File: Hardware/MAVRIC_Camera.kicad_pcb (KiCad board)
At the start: 2 copper layers, 65 x 50 mm, 13 parts, among them J1 MASTER, J2 CAMERA, J3 SERVO, J4 ICSP-PIC, J5 USB, U1 AOZ1031

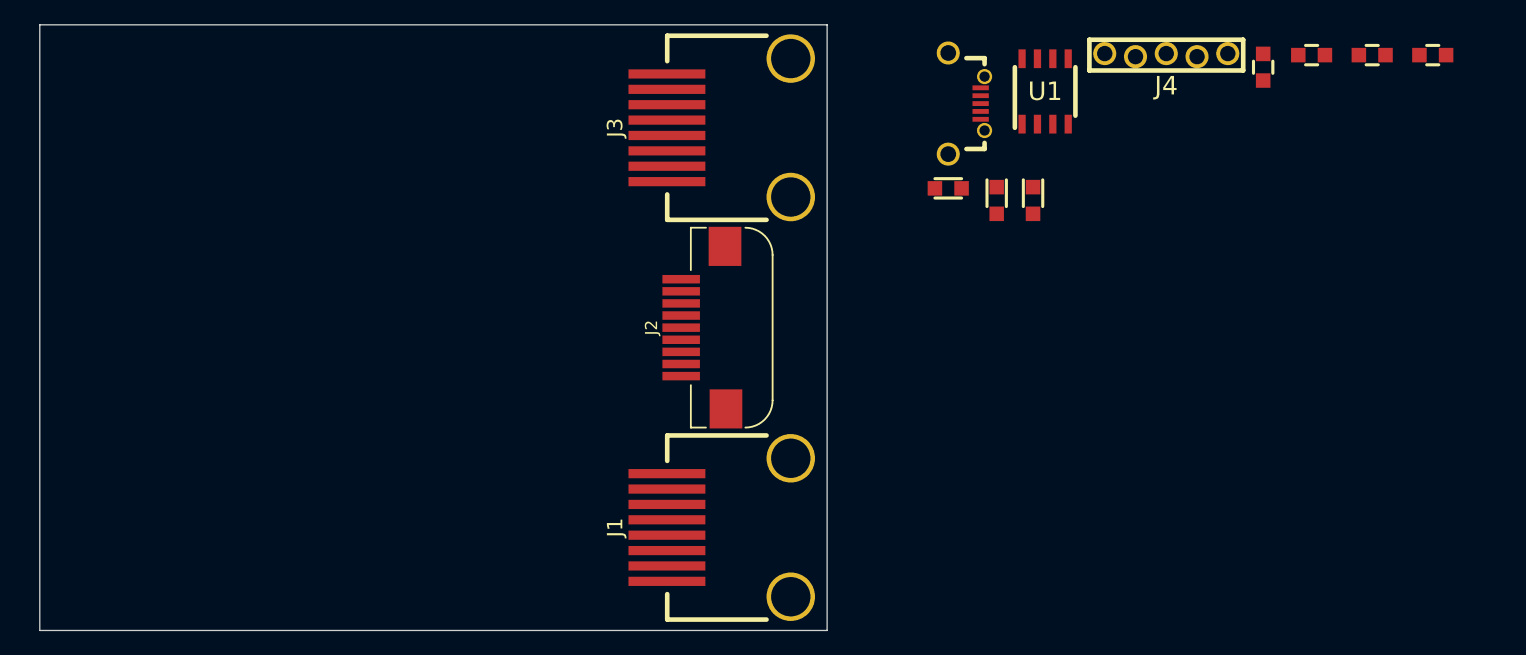
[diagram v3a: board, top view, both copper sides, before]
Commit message: Finish schematic
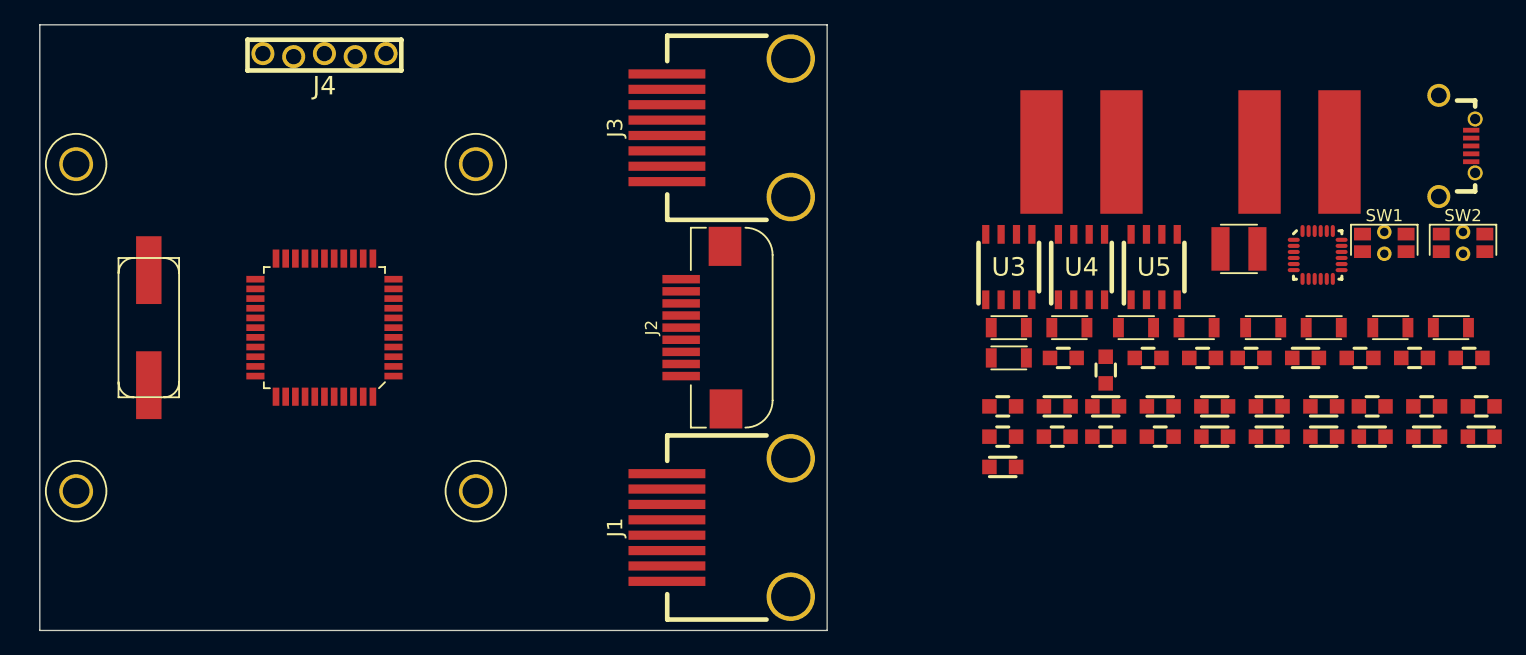
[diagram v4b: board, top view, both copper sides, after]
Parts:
- added C10: 0.1uF, CAPC2012, F.Cu at (239.5, 120.0)
- added C11: 10uF, CAPC2012, F.Cu at (244.0, 122.5)
- added C12: 0.1uF, CAPC2012, F.Cu at (248.5, 122.5)
- added C13: 0.1uF, CAPC2012, F.Cu at (253.0, 122.5)
- added C14: 0.1uF, CAPC2012, F.Cu at (253.0, 120.0)
- added C15: 22uF, CAPC3216, F.Cu at (248.0, 113.5)
- added C16: 22uF, CAPC3216, F.Cu at (253.0, 113.5)
- added C17: C, CAPC2012, F.Cu at (248.5, 120.0)
- added C18: 22uF, CAPC3216, F.Cu at (227.0, 116.0)
- added C19: 22uF, CAPC3216, F.Cu at (242.5, 113.5)
- added C20: C, CAPC2012, F.Cu at (244.0, 120.0)
- added C21: 22uF, CAPC3216, F.Cu at (258.5, 113.5)
- added C22: 22uF, CAPC3216, F.Cu at (227.0, 113.5)
- added C23: 22uF, CAPC3216, F.Cu at (237.5, 113.5)
- added C4: 10nF, CAPC2012, F.Cu at (257.0, 122.5)
- added C5: 0.1uF, CAPC2012, F.Cu at (261.5, 122.5)
- added C6: 0.1uF, CAPC2012, F.Cu at (266.0, 122.5)
- added C7: 2.2nF, CAPC2012, F.Cu at (226.5, 125.0)
- added C8: 18pF, CAPC2012, F.Cu at (235.0, 120.0)
- added C9: 18pF, CAPC2012, F.Cu at (231.0, 120.0)
- added L1: 33uH, INDC-SRN4018, F.Cu at (246.0, 107.0)
- added L2: 22uH, INDC-SRN1060, F.Cu at (251.0, 99.0)
- added L3: 22uH, INDC-SRN1060, F.Cu at (233.0, 99.0)
- added MECH-HOLE220: VAL**, MECH-HOLE220, F.Cu at (150.0, 100.0)
- added MECH-HOLE220: VAL**, MECH-HOLE220, F.Cu at (150.0, 127.0)
- added MECH-HOLE220: VAL**, MECH-HOLE220, F.Cu at (183.0, 127.0)
- added MECH-HOLE220: VAL**, MECH-HOLE220, F.Cu at (183.0, 100.0)
- added R10: 10k, RESC2012, F.Cu at (226.5, 122.5)
- added R11: R, RESC2012, F.Cu at (231.0, 122.5)
- added R12: R, RESC2012, F.Cu at (235.0, 122.5)
- added R13: 10k, RESC2012, F.Cu at (231.5, 116.0)
- added R14: R, RESC2012, F.Cu at (266.0, 120.0)
- added R15: R, RESC2012, F.Cu at (257.0, 120.0)
- added R16: R, RESC2012, F.Cu at (261.5, 120.0)
- added R5: 10k, RESC2012, F.Cu at (260.5, 116.0)
- added R6: 10k, RESC2012, F.Cu at (256.0, 116.0)
- added R7: 10k, RESC2012, F.Cu at (226.5, 120.0)
- added R8: 10k, RESC2012, F.Cu at (265.0, 116.0)
- added R9: R, RESC2012, F.Cu at (239.5, 122.5)
- added SW1: PRGM, SW-EVQP7, F.Cu at (258.0, 106.5)
- added SW2: RESET, SW-EVQP7, F.Cu at (264.5, 106.5)
- added U2: MPU9150, PQFN50P400X400X110-24N, F.Cu at (252.5, 107.5)
- added U3: AOZ1031, SOIC127P600X175-8N, F.Cu at (227.0, 108.5)
- added U4: AOZ1031, SOIC127P600X175-8N, F.Cu at (233.0, 108.5)
- added U5: AOZ1031, SOIC127P600X175-8N, F.Cu at (239.0, 108.5)
- added X1: 8MHz, HC49-US, F.Cu at (156.0, 113.5)
- C1, C2: value CP -> 22uF; footprint CAPCP2012 -> CAPC3216
- J5: value USB -> USB_MINI
- R2: value R -> 10k
- U1: value AOZ1031 -> PIC32MX250F128D; footprint SOIC127P600X175-8N -> QFP80P1200x1200-44N
- moved J4 69.5 mm to (170.5, 91.0)
- moved U1 62.6 mm to (170.5, 113.5), turned to 180 degrees
- moved J5 40.7 mm to (262.5, 98.5)
- moved C2 36.1 mm to (263.5, 113.5), turned to 0 degrees
- moved C3 32.7 mm to (251.5, 116.0)
- moved R4 29.2 mm to (247.0, 116.0)
- moved R3 28.7 mm to (243.0, 116.0)
- moved R2 28.4 mm to (238.5, 116.0)
- moved R1 28.2 mm to (235.0, 117.0)
- moved C1 12.1 mm to (232.0, 113.5), turned to 0 degrees
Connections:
- C1 pad 1: N-000004 -> +3.3V
- C2 pad 1: +BATT -> +3.3V
- J1 pad 2: GND -> AGND
- J1 pad 3: (no net) -> /U1Rx
- J1 pad 6: (no net) -> /U1Tx
- J2 pad 1: (no net) -> /U2Tx
- J2 pad 2: (no net) -> /U2Rx
- J2 pad 4: (no net) -> N-0000028
- J2 pad 7: GND -> AGND
- J3 pad 1: (no net) -> /Pan
- J3 pad 3: (no net) -> /Tilt
- J3 pad 4: N-000004 -> N-0000061
- J3 pad 5: N-000004 -> N-0000061
- J4 pad 1: (no net) -> /~MCLR
- J4 pad 2: (no net) -> +3.3V
- J4 pad 3: (no net) -> GND
- J4 pad 4: (no net) -> /PGD
- J4 pad 5: (no net) -> /PGC
- J5 pad 1: (no net) -> /VBus
- J5 pad 2: (no net) -> /D-
- J5 pad 3: (no net) -> /D+
- J5 pad 5: (no net) -> GND
- R1 pad 1: N-000003 -> N-0000065
- R1 pad 2: N-000004 -> N-0000061
- R3 pad 2: N-000001 -> N-0000063
- R4 pad 2: N-000003 -> N-0000065
- U1 pad 1: GND -> /CamEn
- U1 pad 2: +BATT -> /ServoEn
- U1 pad 3: GND -> /Tilt
- U1 pad 4: N-000003 -> /Pan
- U1 pad 5: N-000001 -> (no net)
- U1 pad 6: /ServoEn -> GND
- U1 pad 7: N-000004 -> /VCap
- U1 pad 8: N-000004 -> /D+

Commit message: Power systems layout
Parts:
- added C24: 22uF, CAPC3216, F.Cu at (191.0, 128.0)
- added C25: 22uF, CAPC3216, F.Cu at (193.5, 128.0)
- L2, L3: footprint INDC-SRN1060 -> INDC-NR8040
- moved SW2 115.5 mm to (149.0, 105.5), turned to 90 degrees
- moved J5 114.5 mm to (149.0, 113.5)
- moved SW1 110.0 mm to (149.0, 92.0), turned to 90 degrees
- moved C2 93.8 mm to (172.0, 134.0), turned to 270 degrees
- moved R14 81.7 mm to (185.5, 134.0)
- moved C3 77.5 mm to (176.5, 96.5), turned to 0 degrees
- moved R16 76.9 mm to (185.5, 132.0), turned to 180 degrees
- moved L1 75.8 mm to (173.5, 129.0), turned to 270 degrees
- moved R4 73.7 mm to (176.5, 94.5)
- moved C17 72.3 mm to (176.5, 113.5)
- moved R15 71.9 mm to (185.5, 128.0), turned to 180 degrees
- moved C15 71.0 mm to (180.5, 135.5)
- moved R3 68.8 mm to (176.5, 98.5)
- moved C21 68.6 mm to (191.0, 101.0), turned to 270 degrees
- moved R9 64.3 mm to (176.5, 109.5), turned to 180 degrees
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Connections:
- net N-0000027 renamed /Lx
- net N-0000030 renamed /CamLx
- net N-0000061 renamed /SevPwr
- net N-0000066 renamed /SevLx
- C16 pad 1: N-0000028 (its old number) -> /CamPwr
- C18 pad 1: N-0000028 (its old number) -> /CamPwr
- J1 pad 1: /Video -> AGND
- J1 pad 2: AGND -> /Video
- J2 pad 4: N-0000028 (its old number) -> /CamPwr
- L2 pad 2: N-0000028 (its old number) -> /CamPwr
- R9 pad 2: N-0000028 (its old number) -> /CamPwr
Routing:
- net AGND: track 0.00 -> 32.3 mm
- net /Video: track 0.00 -> 29.7 mm
- net +BATT: track 0.00 -> 10.9 mm, vias 0 -> 1
- net /SevPwr: track 0.00 -> 9.85 mm
- net N-0000014: track 0.00 -> 4.35 mm
- net /ServoEn: track 0.00 -> 4.35 mm
- net /CamEn: track 0.00 -> 4.35 mm
- net N-0000013: track 0.00 -> 4.12 mm
- net N-0000039: track 0.00 -> 4.12 mm
- net N-0000019: track 0.00 -> 4.12 mm
- net N-0000037: track 0.00 -> 2.28 mm
- net N-0000028: track 0.00 -> 2.28 mm
- net N-0000017: track 0.00 -> 2.28 mm
- net N-0000038: track 0.00 -> 2.00 mm
- net N-0000029: track 0.00 -> 2.00 mm
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- added copper zone on F.Cu, net +3.3V
- added copper zone on F.Cu, net /CamLx
- added copper zone on F.Cu, net /CamPwr
- added copper zone on F.Cu, net /Lx
- added copper zone on F.Cu, net /SevLx
- added copper zone on F.Cu, net /SevPwr
- added copper zone on F.Cu, net GND

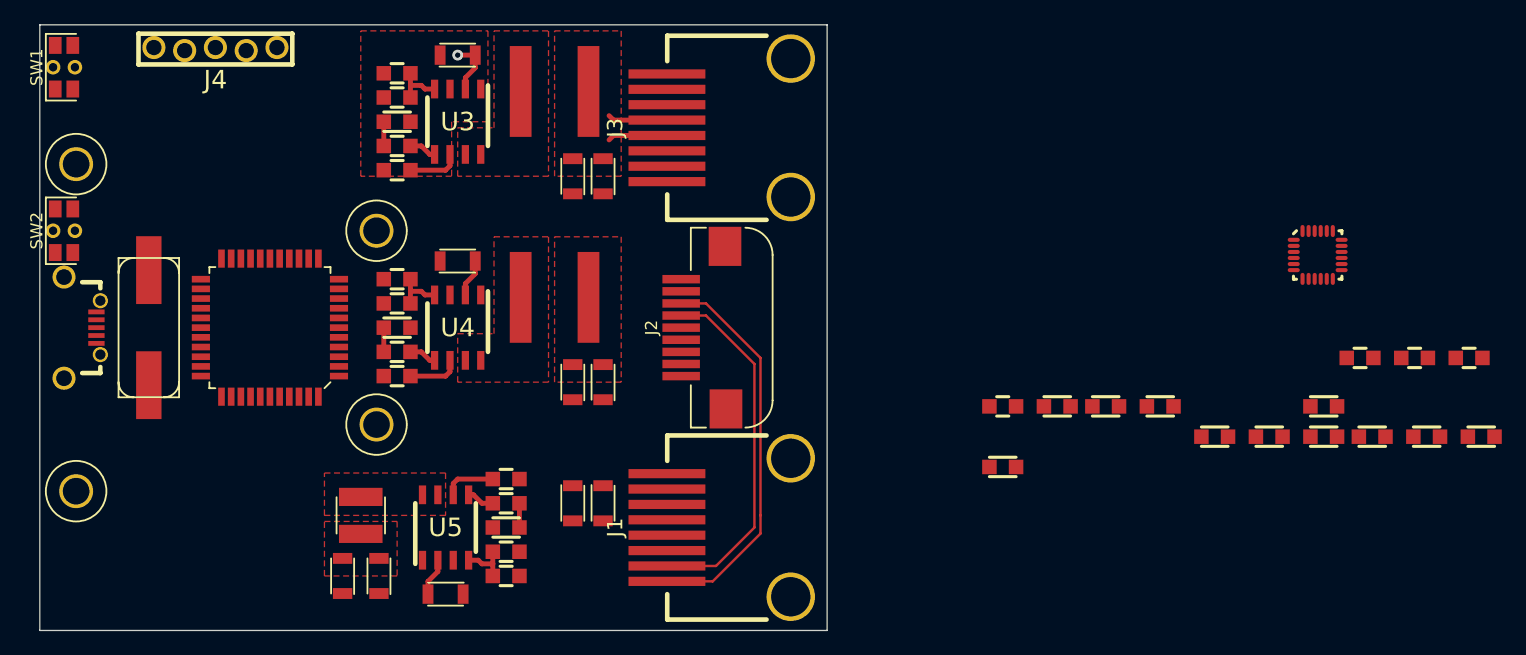
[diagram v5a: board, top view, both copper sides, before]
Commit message: Reload packages for 3d models
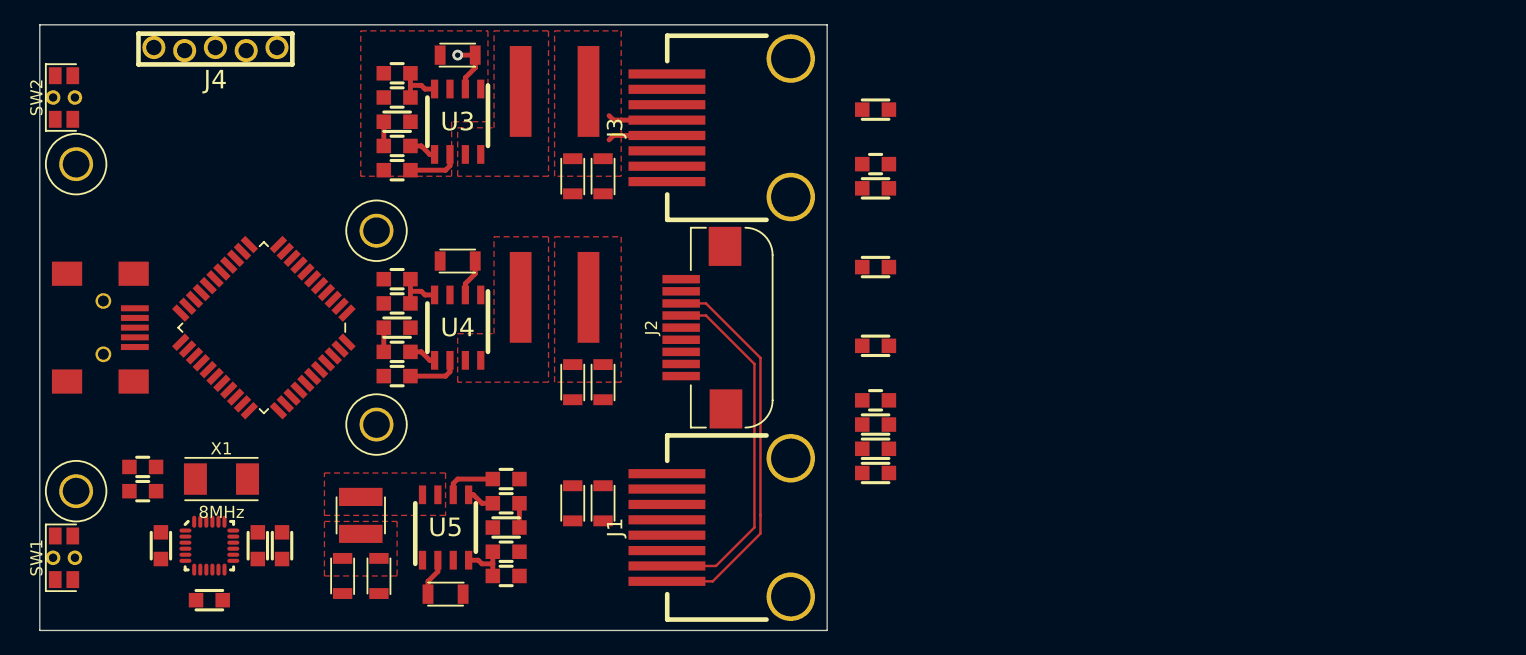
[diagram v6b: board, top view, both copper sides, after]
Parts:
- J1, J3: footprint WM5576 -> CONN-WM5576
- J5: footprint WM17143CT -> CONN-USB-M26FTR
- U3, U4, U5: footprint SOIC127P600X175-8N -> SOIC127P600-8N
- X1: footprint HC49-US -> XTAL-2SMD-60x35
- moved C6 105.9 mm to (161.0, 136.0)
- moved R5 105.4 mm to (155.5, 125.0), turned to 180 degrees
- moved C5 104.9 mm to (157.0, 131.5), turned to 90 degrees
- moved R6 101.1 mm to (155.5, 127.0), turned to 180 degrees
- moved U2 94.6 mm to (161.0, 131.5)
- moved C4 92.4 mm to (165.0, 131.5), turned to 90 degrees
- moved C7 59.9 mm to (167.0, 131.5), turned to 270 degrees
- moved R8 49.1 mm to (216.0, 119.5)
- moved C14 41.1 mm to (216.0, 102.0)
- moved SW1 40.5 mm to (149.0, 132.5)
- moved C13 39.6 mm to (216.0, 108.5)
- moved C11 38.9 mm to (216.0, 95.5)
- moved C12 33.4 mm to (216.0, 115.0)
- moved C10 23.5 mm to (216.0, 121.5)
- moved R7 22.6 mm to (216.0, 100.0)
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
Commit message: New pinout. Update component layout
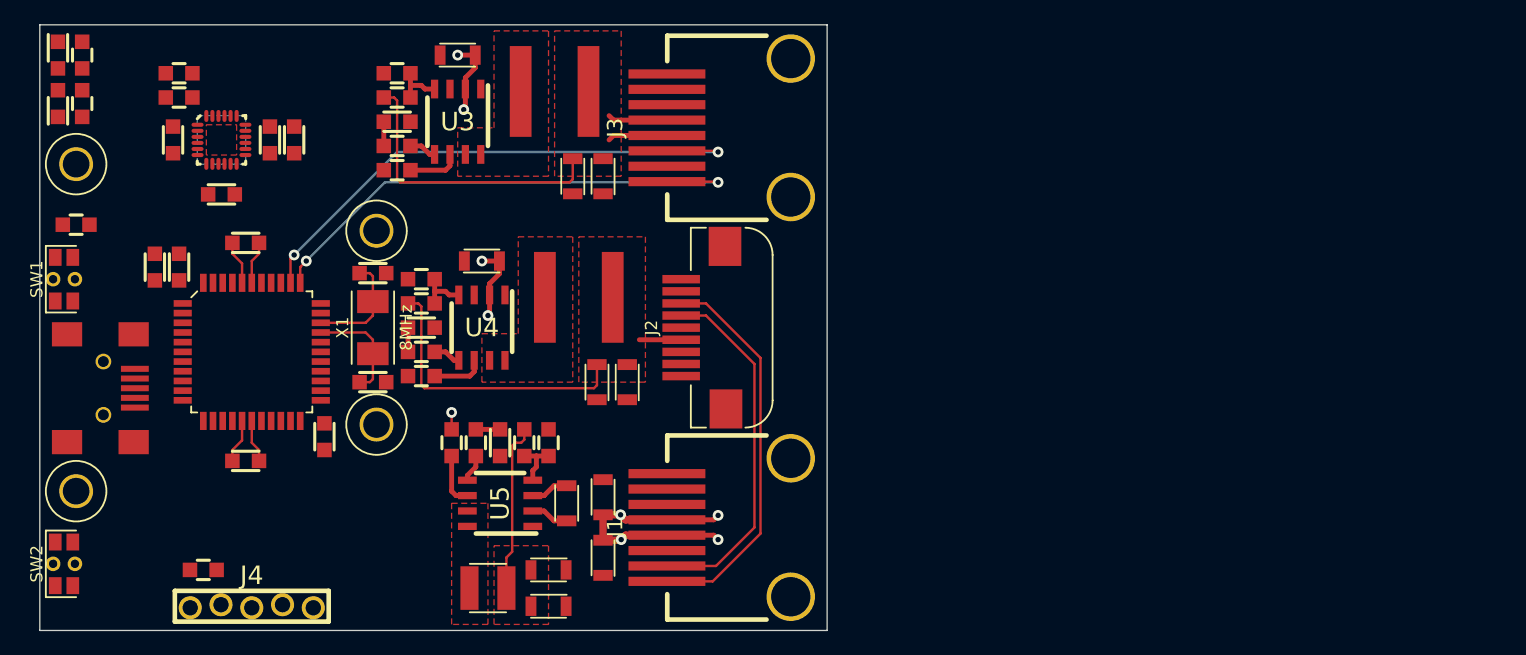
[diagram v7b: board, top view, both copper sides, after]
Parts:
- added D1: LED, LEDC2012, F.Cu at (148.5, 91.0)
- added D2: LED, LEDC2012, F.Cu at (148.5, 95.0)
- added R17: R, RESC2012, F.Cu at (150.5, 91.0)
- added R18: R, RESC2012, F.Cu at (150.5, 95.0)
- moved R7 66.2 mm to (150.0, 105.0)
- moved C11 60.9 mm to (156.5, 108.5), turned to 90 degrees
- moved C10 59.0 mm to (158.5, 108.5), turned to 90 degrees
- moved R8 57.2 mm to (160.5, 133.5)
- moved C12 52.9 mm to (164.0, 124.5), turned to 180 degrees
- moved C14 52.2 mm to (164.0, 106.5)
- moved C13 47.6 mm to (170.5, 122.5), turned to 270 degrees
- moved J4 46.1 mm to (164.5, 136.5), turned to 0 degrees
- moved C9 44.0 mm to (174.5, 109.0)
- moved C8 42.2 mm to (174.5, 118.0)
- moved SW2 38.5 mm to (149.0, 133.0)
- moved C4 33.5 mm to (166.0, 98.0)
- moved C5 33.5 mm to (158.0, 98.0)
- moved C6 33.5 mm to (162.0, 102.5), turned to 180 degrees
- moved C7 33.5 mm to (168.0, 98.0)
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- renumbered MECH-HOLE220 to MECH-HOLE220-1, MECH-HOLE220 to MECH-HOLE220-2, MECH-HOLE220 to MECH-HOLE220-3, MECH-HOLE220 to MECH-HOLE220-4
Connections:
- U1 pad 1: /CamEn -> (no net)
- U1 pad 2: /ServoEn -> (no net)
- U1 pad 25: (no net) -> /U1Tx
- U1 pad 26: (no net) -> /U1Rx
- U1 pad 27: (no net) -> /CamEn
- U1 pad 3: /Tilt -> (no net)
- U1 pad 33: /U1Rx -> (no net)
- U1 pad 34: /U1Tx -> /Pan
- U1 pad 35: (no net) -> /Tilt
- U1 pad 36: (no net) -> /ServoEn
- U1 pad 4: /Pan -> (no net)
- U1 pad 41: (no net) -> /LED
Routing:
- net /Tilt: track 0.00 -> 45.2 mm, vias 0 -> 2
- net /Pan: track 0.00 -> 42.9 mm, vias 0 -> 2
- net +BATT: track 10.9 -> 39.0 mm, vias 1 -> 9
- net /CamPwr: track 0.00 -> 27.6 mm
- net /SevPwr: track 9.85 -> 34.0 mm
- net +3.3V: track 0.00 -> 21.2 mm
- net GND: track 0.00 -> 10.3 mm
- net /OSC2: track 0.00 -> 9.00 mm
- net /OSC1: track 0.00 -> 9.00 mm
- added copper zone on B.Cu, net (none)
- added copper zone on F.Cu, net (none)
- removed copper zone on F.Cu, net GND

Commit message: Completed PCB Design!
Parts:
- moved C13 14.0 mm to (170.5, 108.5), turned to 90 degrees
- moved C7 13.2 mm to (155.0, 96.0), turned to 90 degrees
- moved C6 11.5 mm to (162.0, 91.0), turned to 0 degrees
- moved R6 9.60 mm to (166.0, 100.5), turned to 0 degrees
- moved C4 9.22 mm to (157.0, 96.0), turned to 270 degrees
- moved C5 9.22 mm to (167.0, 96.0), turned to 270 degrees
- moved R5 8.14 mm to (160.0, 100.5)
- moved U2 2.00 mm to (162.0, 96.0), turned to 180 degrees
- moved C1 0.50 mm to (189.0, 133.0)
- moved C15 0.50 mm to (190.5, 127.5)
- moved C2 0.50 mm to (189.0, 136.0)
- moved C20 0.50 mm to (185.0, 122.5)
- moved L1 0.50 mm to (184.0, 134.5)
- moved R13 0.50 mm to (181.0, 122.5)
- moved R14 0.50 mm to (187.0, 122.5)
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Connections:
- J2 pad : (no net) -> GND
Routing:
- net +BATT: track 39.0 -> 164.2 mm
- net /U2Tx: track 0.00 -> 50.1 mm, vias 0 -> 2
- net /U2Rx: track 0.00 -> 48.5 mm, vias 0 -> 2
- net +3.3V: track 21.2 -> 69.4 mm, vias 0 -> 12
- net /U1Tx: track 0.00 -> 36.9 mm, vias 0 -> 2
- net /~MCLR: track 0.00 -> 35.8 mm, vias 0 -> 1
- net /U1Rx: track 0.00 -> 35.0 mm, vias 0 -> 2
- net /PRGM: track 0.00 -> 34.3 mm, vias 0 -> 2
- net /SCL: track 0.00 -> 30.1 mm, vias 0 -> 2
- net /LED: track 0.00 -> 26.5 mm
- net /SDA: track 0.00 -> 26.4 mm, vias 0 -> 2
- net /ServoEn: track 4.35 -> 26.3 mm, vias 0 -> 2
- net /PGC: track 0.00 -> 15.9 mm
- net /PGD: track 0.00 -> 15.4 mm
- net /CamEn: track 4.35 -> 18.8 mm, vias 0 -> 2
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- added copper zone on B.Cu, net +3.3V
- added copper zone on F.Cu, net GND
- removed copper zone on B.Cu, net (none)
- removed copper zone on F.Cu, net (none)
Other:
- board text added: "Back Edge of Camera"
